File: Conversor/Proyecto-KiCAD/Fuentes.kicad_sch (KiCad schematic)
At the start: 19 parts, among them J1 Barrel_Jack_Switch, J8 VDDA Header, J9 5V Header, P2 SW_SPDT, P3 SW_SPDT, P5 5V Header, P6 Jumper 2, U5 LM7805_TO252, U6 THB3-1211, U7 LP2985-3.3

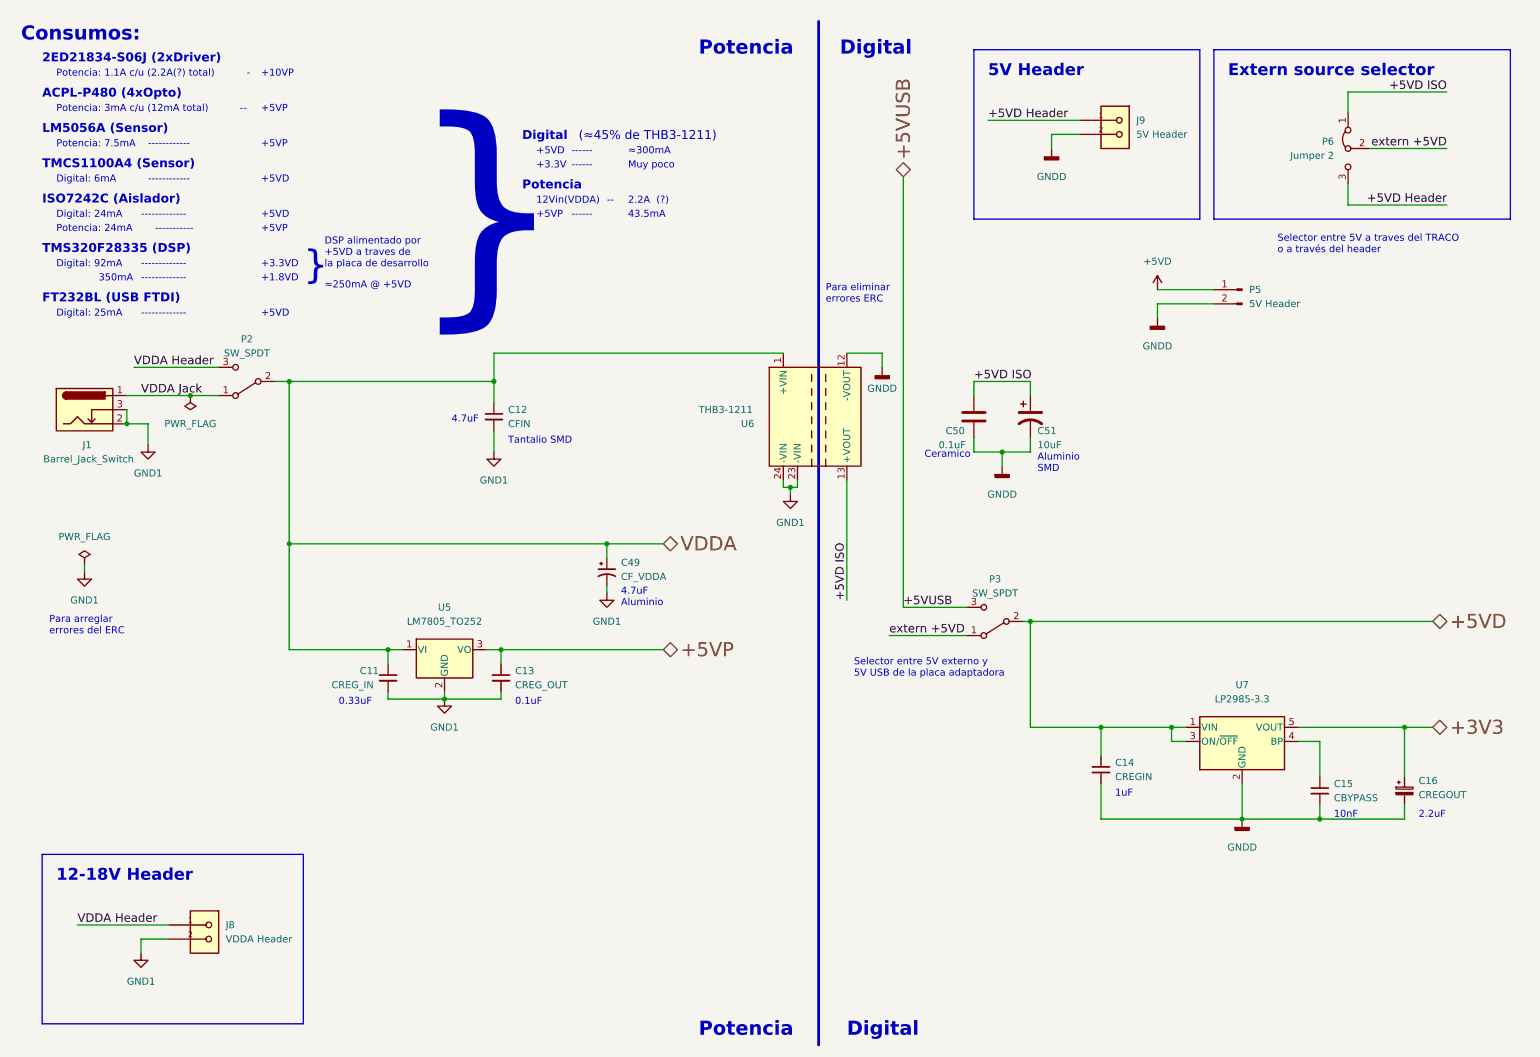
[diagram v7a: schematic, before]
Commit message: Solucionar la union de las lineas de datos I2C
- Segun una evaluation board de Texas, si ya estan separadas las lineas
de I2C como en este caso, solo hay que agregar un adaptador de push-pull
a opne-drain a la salida del aislador
- Se mandó el mail a MayerPCB
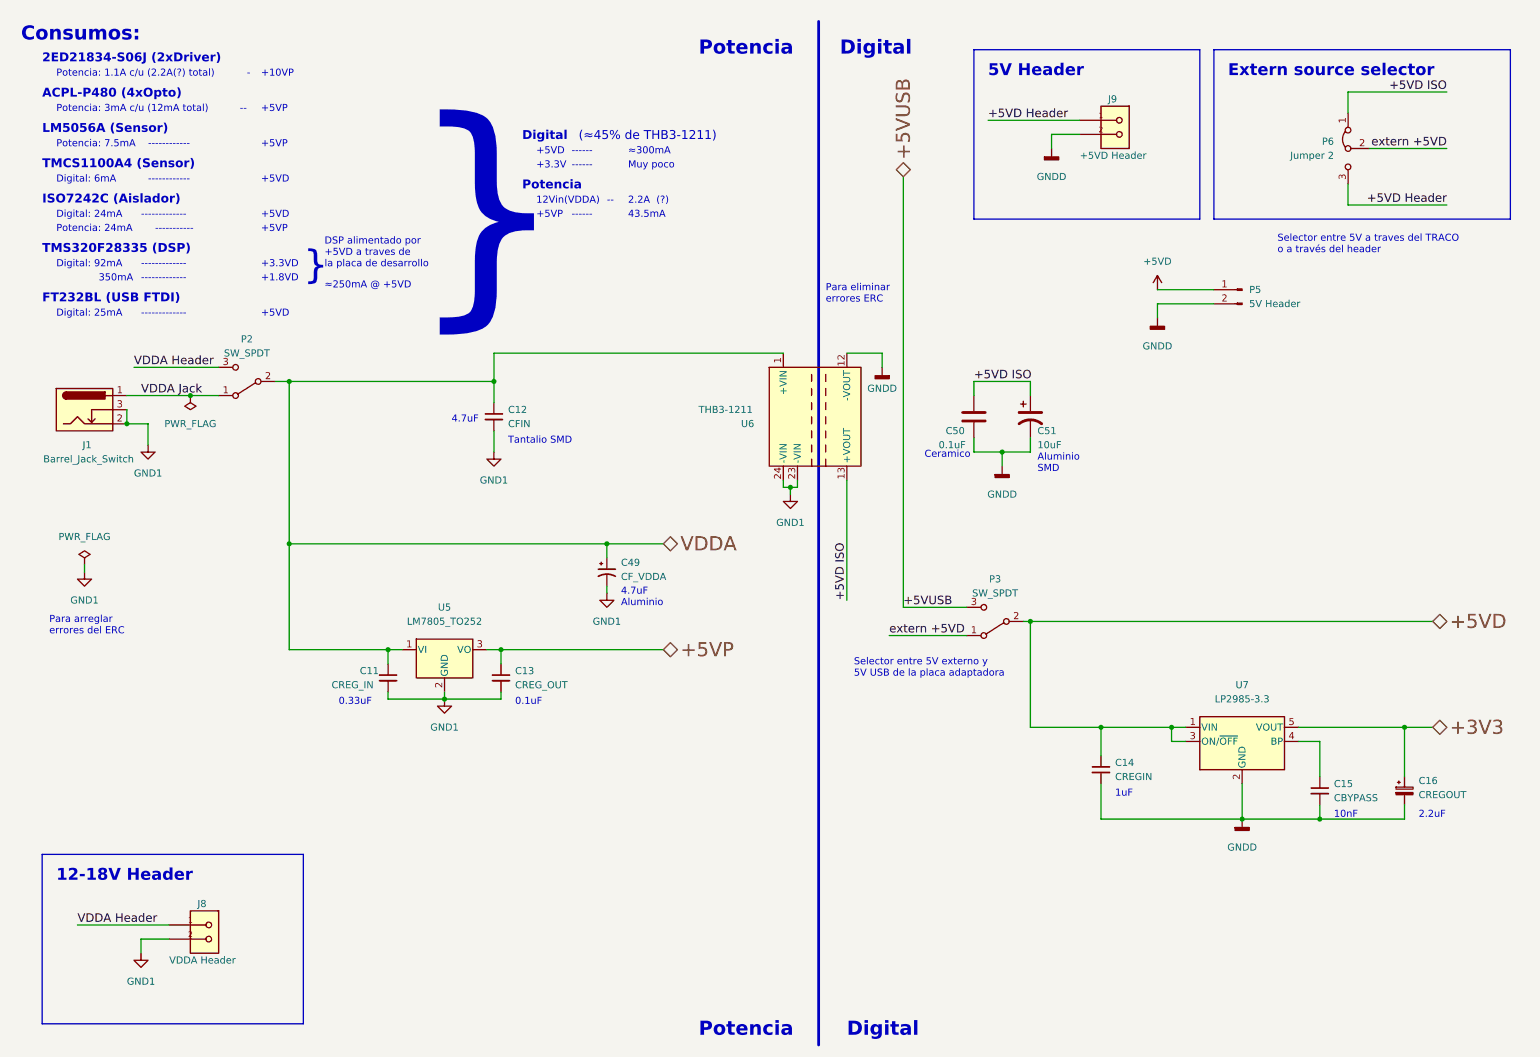
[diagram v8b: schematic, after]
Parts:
- removed J8: VDDA Header, 1725656, symbol 1725656:1725656
- removed J9: 5V Header, 1725656, symbol 1725656:1725656
- added J8: VDDA Header, Phoenix-Contact-2P:Phoenix-Contact-2P, symbol Phoenix-Contact-2P:1725656
- added J9: +5VD Header, Phoenix-Contact-2P:Phoenix-Contact-2P, symbol Phoenix-Contact-2P:1725656
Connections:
- net +5VD Header: now also J9.1
- net GND1: now also J8.2
- net GNDD: now also J9.2
- net VDDA Header: now also J8.1
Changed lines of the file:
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@@
     (pin "1")
-  )
-  (symbol (lib_id "1725656:1725656") (at 208.28 30.48 180) (unit 1)
-    (in_bom yes) (on_board yes) (fields_autoplaced)
-    (property "Reference" "J9" (id 0) (at 213.36 30.4799 0)
-      (effects (font (size 1.27 1.27)) (justify right))
-    )
-    (property "Value" "5V Header" (id 1) (at 213.36 33.0199 0)
-      (effects (font (size 1.27 1.27)) (justify right))
-    )
-    (property "Footprint" "1725656" (id 2) (at 208.28 30.48 0)
-      (effects (font (size 1.27 1.27)) (justify left bottom) hide)
-    )
-    (property "Datasheet" "" (id 3) (at 208.28 30.48 0)
-      (effects (font (size 1.27 1.27)) (justify left bottom) hide)
-    )
-    (pin "1")
-    (pin "2")
   )
   (symbol (lib_id "power:GNDD") (at 189.23 92.71 0) (unit 1)
@@
     (pin "3")
   )
-  (symbol (lib_id "1725656:1725656") (at 44.45 175.26 180) (unit 1)
-    (in_bom yes) (on_board yes) (fields_autoplaced)
-    (property "Reference" "J8" (id 0) (at 49.53 175.2599 0)
-      (effects (font (size 1.27 1.27)) (justify right))
-    )
-    (property "Value" "VDDA Header" (id 1) (at 49.53 177.7999 0)
-      (effects (font (size 1.27 1.27)) (justify right))
-    )
-    (property "Footprint" "1725656" (id 2) (at 44.45 175.26 0)
-      (effects (font (size 1.27 1.27)) (justify left bottom) hide)
-    )
-    (property "Datasheet" "" (id 3) (at 44.45 175.26 0)
-      (effects (font (size 1.27 1.27)) (justify left bottom) hide)
-    )
-    (pin "1")
-    (pin "2")
-  )
   (symbol (lib_id "Device:C_Polarized_Small") (at 261.62 151.13 0) (unit 1)
     (in_bom yes) (on_board yes) (fields_autoplaced)
@@
     (property "Datasheet" "~" (id 3) (at 78.74 130.81 0)
       (effects (font (size 1.27 1.27)) hide)
+    )
+    (pin "1")
+    (pin "2")
+  )
+  (symbol (lib_id "Phoenix-Contact-2P:1725656") (at 208.28 30.48 180) (unit 1)
+    (in_bom yes) (on_board yes)
+    (property "Reference" "J9" (id 0) (at 208.28 26.67 0)
+      (effects (font (size 1.27 1.27)) (justify right))
+    )
+    (property "Value" "+5VD Header" (id 1) (at 203.2 36.83 0)
+      (effects (font (size 1.27 1.27)) (justify right))
+    )
+    (property "Footprint" "Phoenix-Contact-2P:Phoenix-Contact-2P" (id 2) (at 208.28 30.48 0)
+      (effects (font (size 1.27 1.27)) (justify left bottom) hide)
+    )
+    (property "Datasheet" "" (id 3) (at 208.28 30.48 0)
+      (effects (font (size 1.27 1.27)) (justify left bottom) hide)
     )
     (pin "1")
@@
     (pin "1")
   )
+  (symbol (lib_id "Phoenix-Contact-2P:1725656") (at 44.45 175.26 180) (unit 1)
+    (in_bom yes) (on_board yes)
+    (property "Reference" "J8" (id 0) (at 44.45 171.45 0)
+      (effects (font (size 1.27 1.27)) (justify right))
+    )
+    (property "Value" "VDDA Header" (id 1) (at 39.37 181.61 0)
+      (effects (font (size 1.27 1.27)) (justify right))
+    )
+    (property "Footprint" "Phoenix-Contact-2P:Phoenix-Contact-2P" (id 2) (at 44.45 175.26 0)
+      (effects (font (size 1.27 1.27)) (justify left bottom) hide)
+    )
+    (property "Datasheet" "" (id 3) (at 44.45 175.26 0)
+      (effects (font (size 1.27 1.27)) (justify left bottom) hide)
+    )
+    (pin "1")
+    (pin "2")
+  )
   (symbol (lib_id "Device:C_Polarized_Small_US") (at 118.11 111.76 0) (unit 1)
